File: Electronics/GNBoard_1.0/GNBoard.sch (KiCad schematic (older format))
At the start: 47 parts, among them K1 IR1, K10 IR4, K11 CNY_1, K12 CNY_2, K13 CNY_3, K14 CNY_4, K15 CNY_5, K16 CNY_6, K2 IR2, K3 SERVO_1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

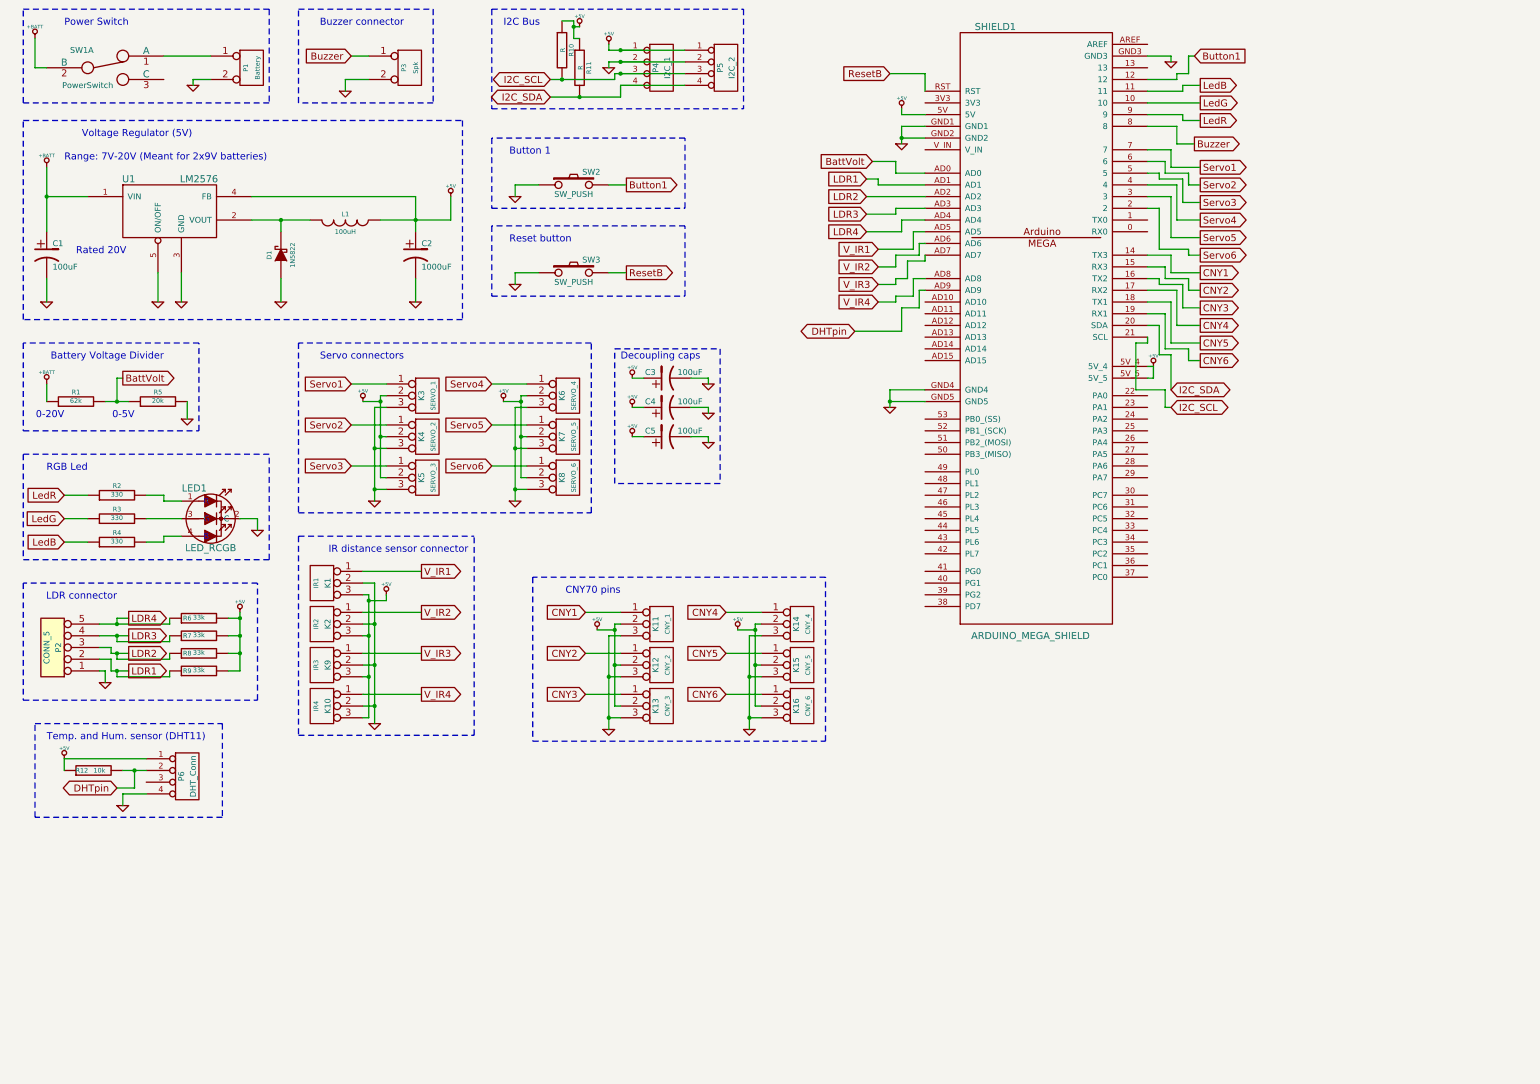
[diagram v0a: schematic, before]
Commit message: Moved v0.1 to its own folder
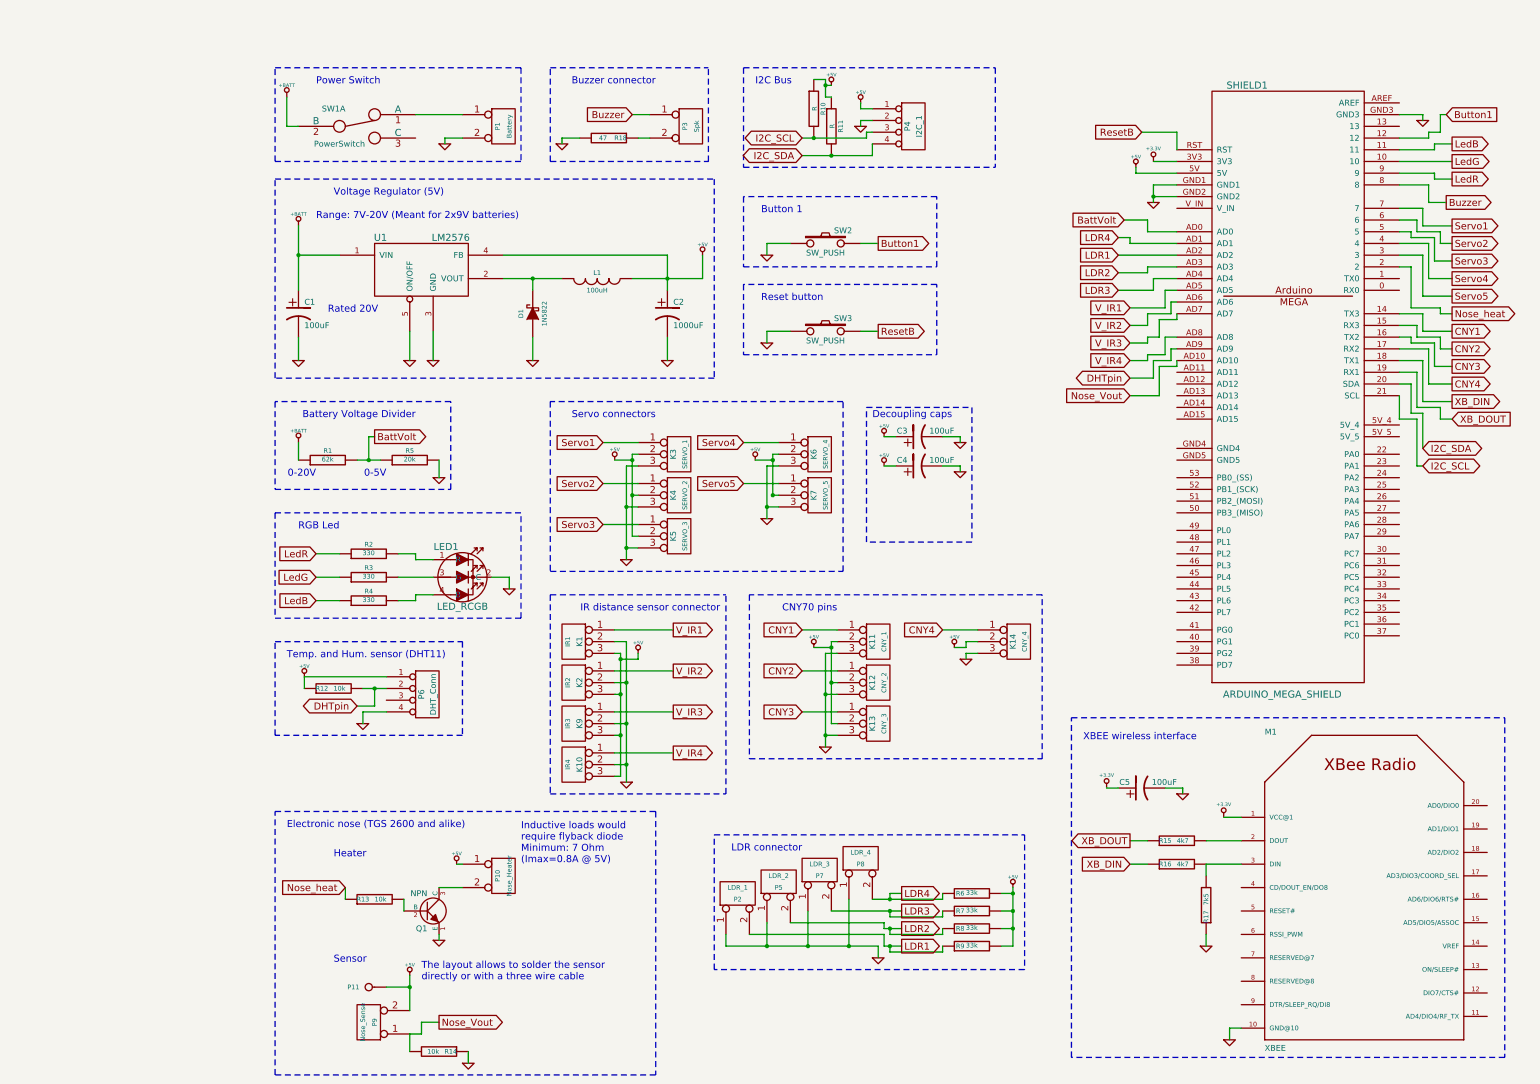
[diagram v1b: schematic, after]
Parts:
- removed K15: CNY_5, ~, symbol CONN_3
- removed K16: CNY_6, ~, symbol CONN_3
- removed K8: SERVO_6, ~, symbol CONN_3
- removed P2: CONN_5, ~, symbol CONN_5
- removed P5: I2C_2, ~, symbol CONN_4
- added M1: XBEE, xbee_r1-XBEE, symbol XBEE
- added P10: Nose_Heater, ~, symbol CONN_2
- added P11: CONN_1, ~, symbol CONN_1
- added P2: LDR_1, ~, symbol CONN_2
- added P5: LDR_2, ~, symbol CONN_2
- added P7: LDR_3, ~, symbol CONN_2
- added P8: LDR_4, ~, symbol CONN_2
- added P9: Nose_Sense, ~, symbol CONN_2
- added Q1: NPN, ~, symbol NPN
- added R13, R14: 10k, ~, symbol R
- added R15, R16: 4k7, ~, symbol R
- added R17: 7k5, ~, symbol R
- added R18: 47, ~, symbol R
- L1: Rated (none) -> 3A
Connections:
- net +5V: now also P10.1 (P1), P11.1, P9.2 (PM); no longer C5.1, SHIELD1.5V_4, SHIELD1.5V_5
- net GND: now also M1.10 (GND@10), P2.1 (P1), P5.1 (P1), P7.1 (P1), P8.1 (P1), Q1.1 (E), R14.1, R17.1, R18.2; no longer P3.2 (PM), SHIELD1.GND4, SHIELD1.GND5
- net LDR1: now also SHIELD1.AD2, P2.2 (PM); no longer SHIELD1.AD1
- net LDR2: now also SHIELD1.AD3, P5.2 (PM); no longer SHIELD1.AD2
- net LDR3: now also SHIELD1.AD4, P7.2 (PM); no longer SHIELD1.AD3
- net LDR4: now also SHIELD1.AD1, P8.2 (PM); no longer SHIELD1.AD4
- net +3.3V: now reaches SHIELD1.3V3
- net +3.3V: now also C5.1, M1.1 (VCC@1)
- net Nose_Vout: now reaches SHIELD1.AD10
- net Nose_Vout: now also P9.1 (P1), R14.2
- net CNY5 renamed XB_DIN
- net XB_DIN: now also R16.1
- net CNY6 renamed XB_DOUT
- net XB_DOUT: now also R15.1
- net Servo6 renamed Nose_heat
- net Nose_heat: now also R13.1
- new net: P3.2 (PM), R18.1
- new net: M1.2 (DOUT), R15.2
- new net: M1.3 (DIN), R16.2, R17.2
- new net: Q1.2 (B), R13.2
- new net: P10.2 (PM), Q1.3 (C)
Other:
- note added: "Electronic nose (TGS 2600 and alike)"
- note added: "Heater"
- note added: "Inductive loads would\nrequire flyback diode\nMinimum: 7 Ohm\n(Imax=0.8A @ 5V)"
- note added: "Sensor"
- note added: "The layout allows to solder the sensor\ndirectly or with a three wire cable"
- note added: "XBEE wireless interface"
- moved on the sheet: C1, C2, C3, C4, C5, D1, K1, K10, K11, K12, K13, K14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

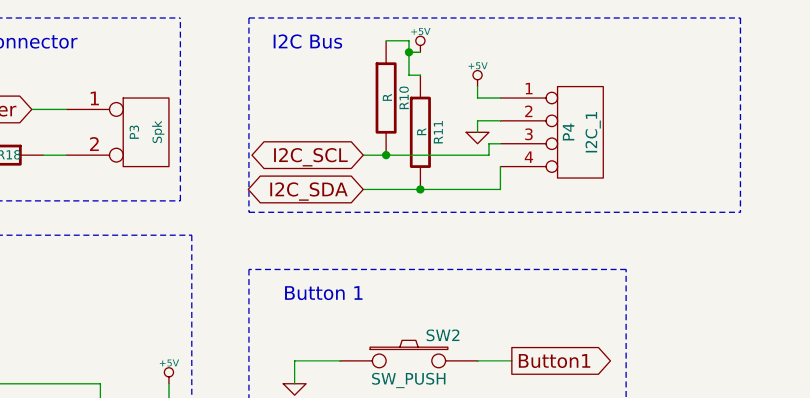
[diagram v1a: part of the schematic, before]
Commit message: Resized silkscreen texts, resistor values are now shown
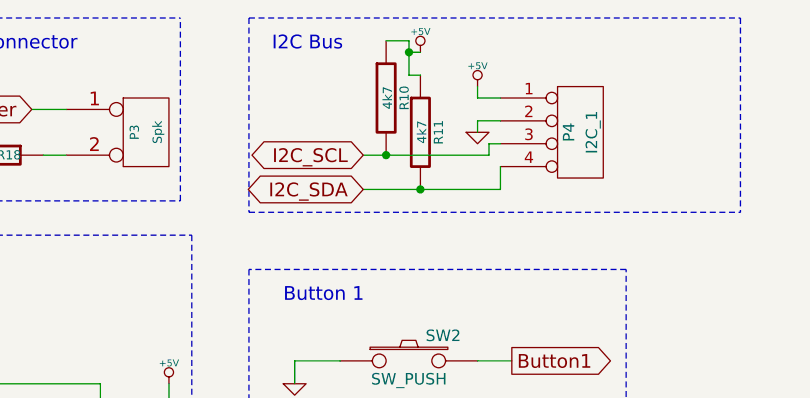
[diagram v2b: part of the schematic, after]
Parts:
- R10, R11: value R -> 4k7
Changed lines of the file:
@@
 Sheet 1 1
 Title "GNBoard (Shield for Arduino Mega)"
-Date "8 feb 2014"
+Date "9 feb 2014"
 Rev ""
 Comp ""
@@
 P 7350 1500
 F 0 "R10" V 7430 1500 40  0000 C CNN
-F 1 "R" V 7357 1501 40  0000 C CNN
+F 1 "4k7" V 7357 1501 40  0000 C CNN
 F 2 "~" V 7280 1500 30  0000 C CNN
 F 3 "~" H 7350 1500 30  0000 C CNN
@@
 P 7500 1650
 F 0 "R11" V 7580 1650 40  0000 C CNN
-F 1 "R" V 7507 1651 40  0000 C CNN
+F 1 "4k7" V 7507 1651 40  0000 C CNN
 F 2 "~" V 7430 1650 30  0000 C CNN
 F 3 "~" H 7500 1650 30  0000 C CNN

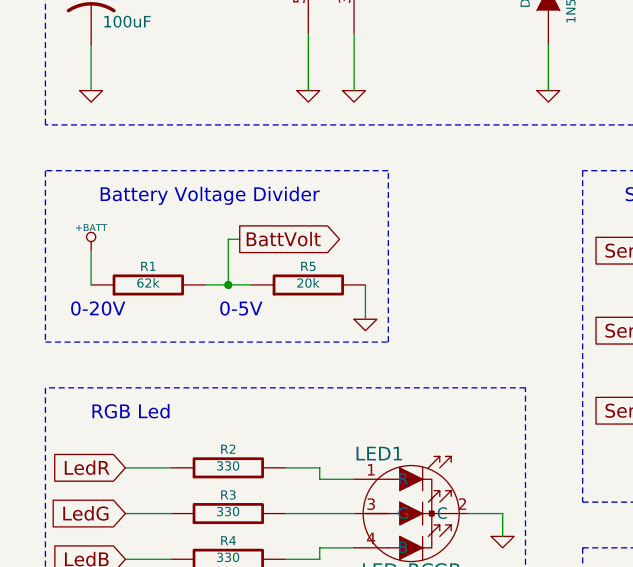
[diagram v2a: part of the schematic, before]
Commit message: Updated value of the resistors for the battery voltage monitor
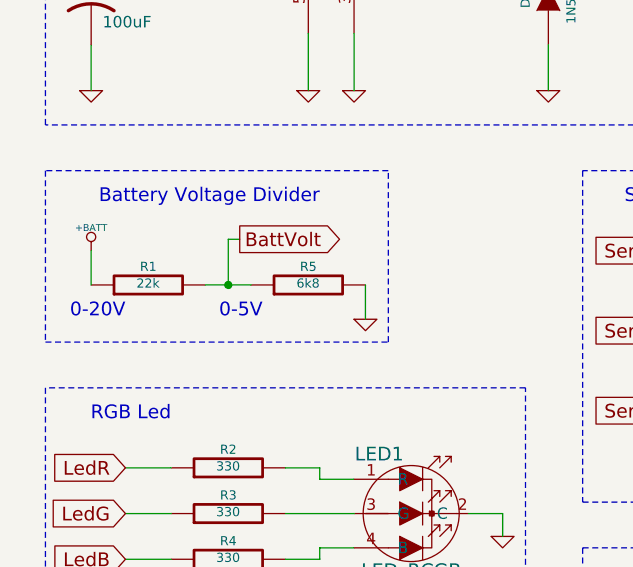
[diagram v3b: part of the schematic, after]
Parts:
- R1: value 62k -> 22k
- R5: value 20k -> 6k8
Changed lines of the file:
@@
 Sheet 1 1
 Title "GNBoard (Shield for Arduino Mega)"
-Date "9 feb 2014"
+Date "10 feb 2014"
 Rev ""
 Comp ""
@@
 P 3200 4500
 F 0 "R1" V 3280 4500 40  0000 C CNN
-F 1 "62k" V 3207 4501 40  0000 C CNN
+F 1 "22k" V 3207 4501 40  0000 C CNN
 F 2 "~" V 3130 4500 30  0000 C CNN
 F 3 "~" H 3200 4500 30  0000 C CNN
@@
 P 3900 4500
 F 0 "R5" V 3980 4500 40  0000 C CNN
-F 1 "20k" V 3907 4501 40  0000 C CNN
+F 1 "6k8" V 3907 4501 40  0000 C CNN
 F 2 "~" V 3830 4500 30  0000 C CNN
 F 3 "~" H 3900 4500 30  0000 C CNN
